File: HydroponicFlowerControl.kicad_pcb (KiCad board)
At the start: 4 copper layers, 101 x 101 mm, 241 parts, among them IC1 ADM3260ARSZ-RL7, IC2 ADM3260ARSZ-RL7, IC3 CH224K, J1 EC, J10 Pump 1, J11 Temperature, J12 Pump 2, J13 Pump 3, J14 D IN1, J15 D IN2, J16 D IN3, J17 CAN, J18 Raspberry_Pi_2_3, J19 Conn_ARM_JTAG_SWD_10, J2 Temp, J20 Conn_ARM_JTAG_SWD_10, J3 Flow, J4 pH, J5 USB_C_Receptacle_USB2.0, J6 Barrel_Jack, J7 Valve 1, J8 Valve 2, J9 Valve 3, Q1 MMBT3904, Q10 AO3401A, Q11 MMBT3904, Q12 AO3401A, Q2 AO3401A, Q3 MMBT3904, Q4 AO3401A, Q5 MMBT3904, Q6 AO3401A, Q7 MMBT3904, Q8 MMBT3904, Q9 AO3401A, SW1 RESET, U1 AT24C256C, U10 REF3020, U11 TPS60400DBV, U12 ADS1115IDGS, U13 TPD2EUSB30, U14 TLV271, U15 TLV271, U16 MCP2518FD-xQBB, U17 HDC1080, U18 SN65HVD230, U19 SN65HVD230, U2 ADS1115IDGS, U20 TPS5430DDA, U4 TPS60400DBV, U5 LM324, U6 MCP4017T-502E/LT, U7 LM358, U8 STM32G473CBTx, U9 AMS1117-3.3, Y1 8 MHz, Y2 40MHz

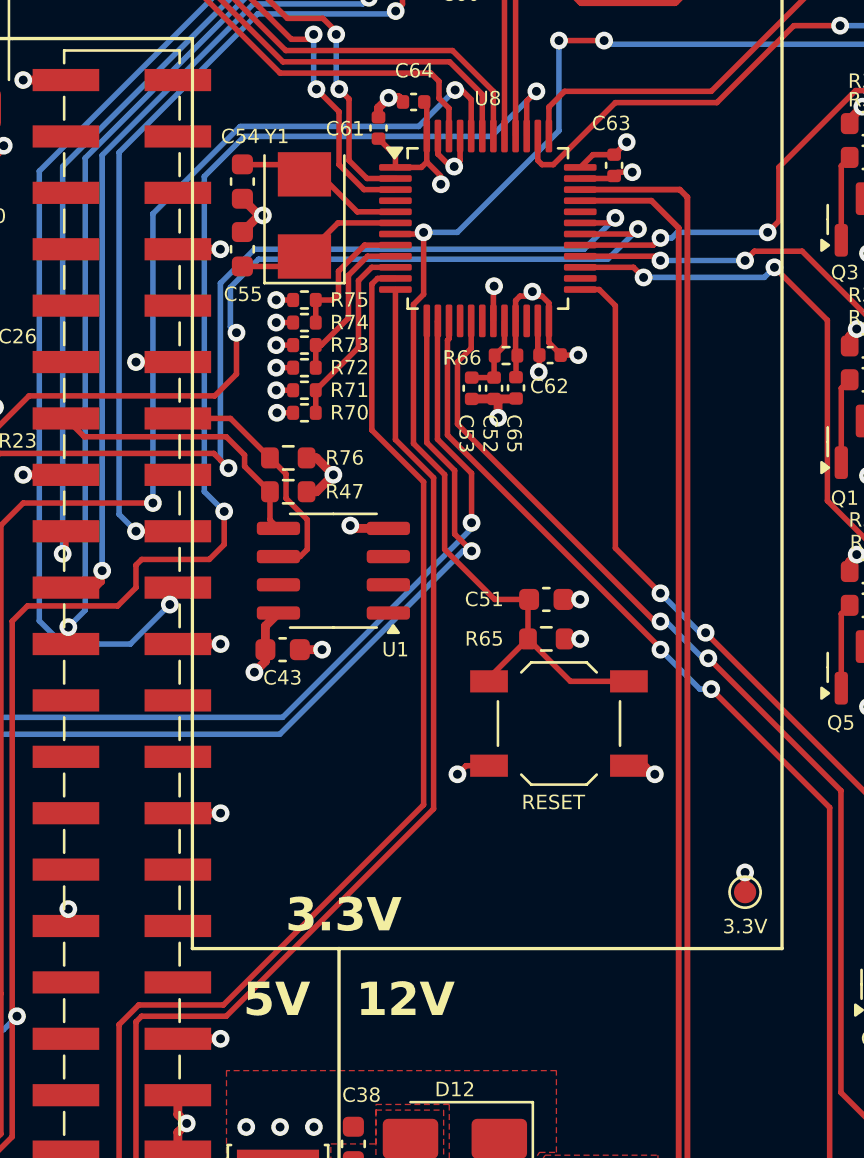
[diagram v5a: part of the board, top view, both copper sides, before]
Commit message: Connect button to BOOT0
This is used to enter DFU bootloader
Closes #26
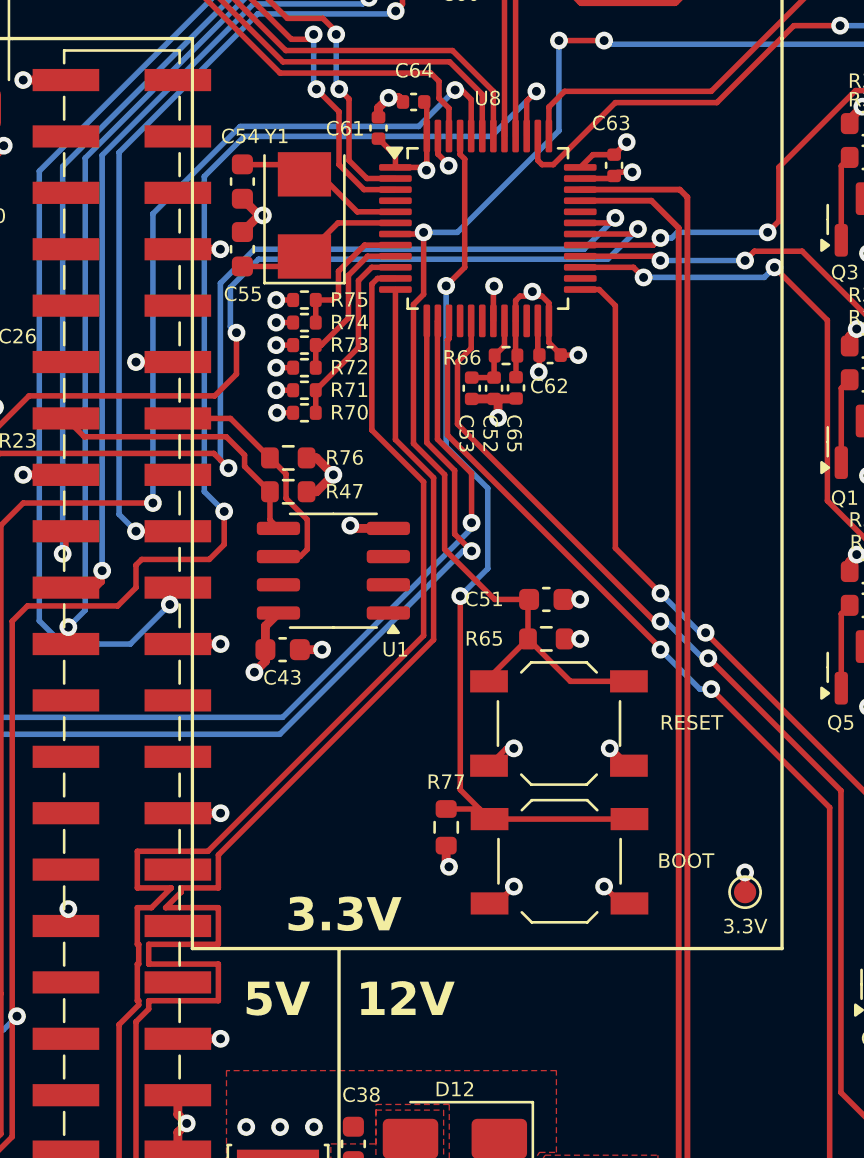
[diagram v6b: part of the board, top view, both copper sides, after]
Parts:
- added R77: 10k, Resistor_SMD:R_0603_1608Metric, F.Cu at (120.5, 114.4)
- added SW2: BOOT, Button_Switch_SMD:SW_SPST_TL3342, F.Cu at (125.6, 115.9)
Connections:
- U8 pad 45: GND -> BOOT0
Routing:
- net BOOT0: track 0.00 -> 41.5 mm, vias 0 -> 2
- net /Flow control/TEMP: track 91.2 -> 101.4 mm
- net /Flow control/FLOW: track 97.8 -> 100.2 mm
- net +3.3V: track 85.5 -> 87.5 mm, vias 22 -> 24
- net GND: track 161.0 -> 160.0 mm, vias 93 -> 94
